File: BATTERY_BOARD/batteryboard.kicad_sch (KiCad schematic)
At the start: 32 parts, among them J1 KEYSTONE-1042, J10 Screw_Terminal_01x02, J11 Screw_Terminal_01x02, J12 Screw_Terminal_01x01, J2 KEYSTONE-1042, J3 KEYSTONE-1042, J4 KEYSTONE-1042, J5 KEYSTONE-1042, J6 KEYSTONE-1042, J7 JST_PH_S2B-PH-SM4, J8 Screw_Terminal_01x02, J9 Screw_Terminal_01x02, Q1 IRF7458, Q2 IRF7458, U1 R5460N233AF

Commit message: Battery Board Final Update
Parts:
- removed J10, J11, J8, J9: Screw_Terminal_01x02, custom-footprints:SCREWTERMINAL-3.5MM-2_LOCK, symbol Connector:Screw_Terminal_01x02
- removed J12: Screw_Terminal_01x01, Connector_PinHeader_1.00mm:PinHeader_1x01_P1.00mm_Vertical, symbol Connector:Screw_Terminal_01x01
- removed J7: JST_PH_S2B-PH-SM4, Connector_JST:JST_PH_S2B-PH-SM4-TB_1x02-1MP_P2.00mm_Horizontal, symbol Connector:Screw_Terminal_01x02
- added D4: DFLS130L, mainboard:PWRDI-123, symbol mainboard:DFLS130L
- added J10, J13, J14, J15, J16, J7, J8: SM02B-SFHRS-TF_LF__SN_, SM02BSFHRSTFLFSN, symbol SamacSys_Parts:SM02B-SFHRS-TF_LF__SN_
- added J11: F3311A7H121014E200, F3311A7H121014E200, symbol SamacSys_Parts:F3311A7H121014E200
- added K1: 9-1462038-9, 914620389, symbol SamacSys_Parts:9-1462038-9
- added Q20 (x2), Q21 (x2): NDS8434, mainboard:NDS8434, symbol mainboard:NDS8434
- added Q4 (x2), Q5 (x2): IRLML2803, mainboard:SOT-23, symbol mainboard:IRLML2803TRPBF
- added Q6: MMBT2222AT, mainboard:SOT-23, symbol mainboard:MMBT2222AT
- added R25, R27 (x2), R28 (x2): 10k, Resistor_SMD:R_0603_1608Metric, symbol mainboard:RESISTOR0603
- added R32 (x2), R33 (x2): 4.7k, Resistor_SMD:R_0603_1608Metric, symbol mainboard:RESISTOR0603
- added R37 (x2), R38 (x2): 100k, Resistor_SMD:R_0603_1608Metric, symbol mainboard:RESISTOR0603
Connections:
- net BAT_THERM: now also J11.13
- net PACK+: now also J10.2, J7.2
- net PACK- renamed GND
- net GND: now also J10.1, J11.14, J11.7, J13.1, J14.1, J15.1, J16.1, J7.1, K1.7 (NC_2), Q4.2 (S), Q4.2 (S), Q5.2 (S), Q5.2 (S), Q6.2 (E), R25.2, R27.2, R27.2, R28.2, R28.2
- new net: D4.A, K1.8 (COIL-), Q6.3 (C)
- new net: Q20.4 (Gate), Q4.3 (D), R37.1 (x2)
- new net: Q21.4 (Gate), Q5.3 (D), R38.1 (x2)
- new net: Q5.1 (G), R33.1 (x2)
- new net: Q4.1 (G), R32.1 (x2)
- new net BURN_RELAY_A: J11.8, Q6.1 (B), R25.1
- new net ENAB_BURN1: J11.9, R27.1, R32.2
- new net ENAB_BURN2: J11.10, R28.1, R33.2
- new net ENAB_BURN3: J11.11, R28.1, R33.2
- new net ENAB_BURN4: J11.12, R27.1, R32.2
- new net VBATT: D4.C, J8.1, J8.2, K1.1 (COIL+), K1.5 (NO_2)
- new net VBURN1: J14.2, Q20.5 (Drain), Q20.6 (Drain), Q20.7 (Drain), Q20.8 (Drain)
- new net VBURN2: J13.2, Q21.5 (Drain), Q21.6 (Drain), Q21.7 (Drain), Q21.8 (Drain)
- new net VBURN3: J15.2, Q21.5 (Drain), Q21.6 (Drain), Q21.7 (Drain), Q21.8 (Drain)
- new net VBURN4: J16.2, Q20.5 (Drain), Q20.6 (Drain), Q20.7 (Drain), Q20.8 (Drain)
- new net VBURN_A_IN: K1.6 (COM_2), Q20.1 (Source), Q20.1 (Source), Q20.2 (Source), Q20.2 (Source), Q20.3 (Source), Q20.3 (Source), Q21.1 (Source), Q21.1 (Source), Q21.2 (Source), Q21.2 (Source), Q21.3 (Source), Q21.3 (Source), R37.2, R37.2, R38.2, R38.2
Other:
- note added: "Burn Wire Control (Antenna Depolyment)"
- note added: "NOTE: Components labeled "do not install" (DNI) are not populated by default"
- note added: "Power Relay A"
- note removed: "Vertical or horizontal JST_PH"
- moved on the sheet: C1, C2, C3, C4, H1, H2, H3, H4, J1, J2, J3, J4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

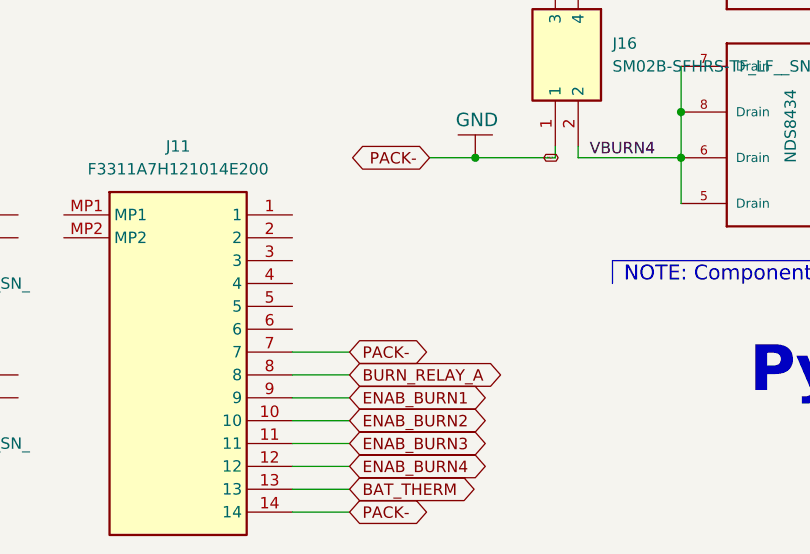
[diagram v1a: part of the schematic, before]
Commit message: Updated the FPC Connections
FPC connector is reversable now
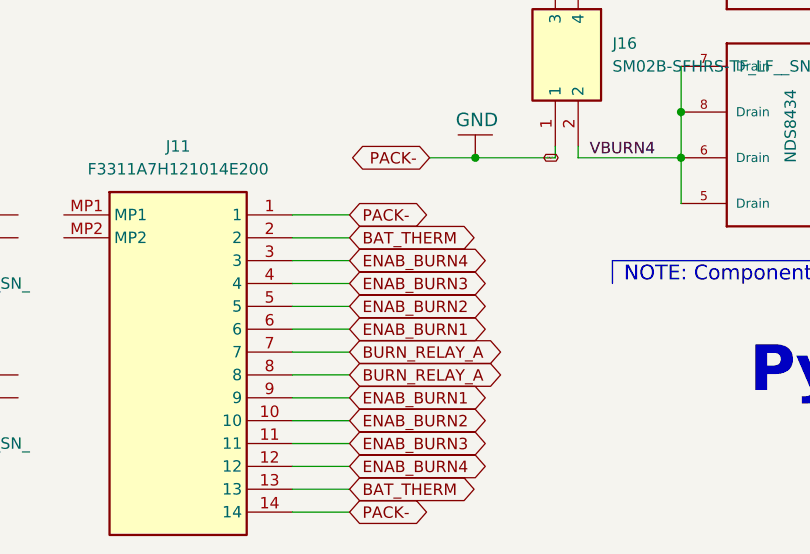
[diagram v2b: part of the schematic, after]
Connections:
- net BAT_THERM: now also J11.2
- net BURN_RELAY_A: now also J11.7
- net ENAB_BURN1: now also J11.6
- net ENAB_BURN2: now also J11.5
- net ENAB_BURN3: now also J11.4
- net ENAB_BURN4: now also J11.3
- net GND: now also J11.1; no longer J11.7
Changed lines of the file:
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@@
   (no_connect (at 44.45 151.13))
   (no_connect (at 44.45 135.89))
+  (wire (pts (xy 123.19 171.45) (xy 129.54 171.45))
+    (stroke (width 0) (type default))
+  )
   (wire (pts (xy 166.37 157.48) (xy 166.37 152.4))
     (stroke (width 0) (type default))
@@
     (stroke (width 0) (type default))
   )
+  (wire (pts (xy 123.19 173.99) (xy 129.54 173.99))
+    (stroke (width 0) (type default))
+  )
   (wire (pts (xy 198.12 99.06) (xy 205.74 99.06))
     (stroke (width 0) (type default))
@@
     (stroke (width 0) (type default))
   )
+  (wire (pts (xy 123.19 168.91) (xy 129.54 168.91))
+    (stroke (width 0) (type default))
+  )
   (wire (pts (xy 223.52 77.47) (xy 223.52 74.93))
     (stroke (width 0) (type default))
@@
     (stroke (width 0) (type default))
   )
+  (wire (pts (xy 123.19 179.07) (xy 129.54 179.07))
+    (stroke (width 0) (type default))
+  )
   (wire (pts (xy 213.36 82.55) (xy 213.36 87.63))
     (stroke (width 0) (type default))
@@
     (stroke (width 0) (type default))
   )
+  (wire (pts (xy 123.19 176.53) (xy 129.54 176.53))
+    (stroke (width 0) (type default))
+  )
   (wire (pts (xy 34.29 50.8) (xy 34.29 39.37))
     (stroke (width 0) (type default))
@@
     (stroke (width 0) (type default))
   )
-  (wire (pts (xy 123.19 179.07) (xy 129.54 179.07))
-    (stroke (width 0) (type default))
-  )
   (wire (pts (xy 205.74 104.14) (xy 205.74 101.6))
     (stroke (width 0) (type default))
@@
     (stroke (width 0) (type default))
   )
+  (wire (pts (xy 123.19 166.37) (xy 129.54 166.37))
+    (stroke (width 0) (type default))
+  )
   (wire (pts (xy 138.43 157.48) (xy 143.51 157.48))
     (stroke (width 0) (type default))
@@
   )
   (wire (pts (xy 161.29 85.09) (xy 172.72 85.09))
+    (stroke (width 0) (type default))
+  )
+  (wire (pts (xy 123.19 163.83) (xy 129.54 163.83))
     (stroke (width 0) (type default))
   )
@@
     )
   )
+  (global_label "PACK-" (shape bidirectional) (at 129.54 163.83 0)
+    (effects (font (size 1.27 1.27)) (justify left))
+    (property "Intersheetrefs" "${INTERSHEET_REFS}" (at 129.54 163.83 0)
+      (effects (font (size 1.27 1.27)) hide)
+    )
+  )
+  (global_label "BURN_RELAY_A" (shape bidirectional) (at 129.54 179.07 0)
+    (effects (font (size 1.27 1.27)) (justify left))
+    (property "Intersheetrefs" "${INTERSHEET_REFS}" (at 129.54 179.07 0)
+      (effects (font (size 1.27 1.27)) hide)
+    )
+  )
   (global_label "PACK+" (shape bidirectional) (at 100.33 104.14 270)
     (effects (font (size 1.27 1.27)) (justify right))
@@
     )
   )
+  (global_label "ENAB_BURN3" (shape bidirectional) (at 129.54 171.45 0)
+    (effects (font (size 1.27 1.27)) (justify left))
+    (property "Intersheetrefs" "${INTERSHEET_REFS}" (at 129.54 171.45 0)
+      (effects (font (size 1.27 1.27)) hide)
+    )
+  )
   (global_label "ENAB_BURN2" (shape bidirectional) (at 226.06 87.63 0)
     (effects (font (size 1.27 1.27)) (justify left))
@@
     )
   )
+  (global_label "ENAB_BURN4" (shape bidirectional) (at 129.54 168.91 0)
+    (effects (font (size 1.27 1.27)) (justify left))
+    (property "Intersheetrefs" "${INTERSHEET_REFS}" (at 129.54 168.91 0)
+      (effects (font (size 1.27 1.27)) hide)
+    )
+  )
   (global_label "BM" (shape bidirectional) (at 29.21 180.34 270)
     (effects (font (size 1.27 1.27)) (justify right))
@@
     )
   )
+  (global_label "BAT_THERM" (shape bidirectional) (at 129.54 166.37 0)
+    (effects (font (size 1.27 1.27)) (justify left))
+    (property "Intersheetrefs" "${INTERSHEET_REFS}" (at 129.54 166.37 0)
+      (effects (font (size 1.27 1.27)) hide)
+    )
+  )
   (global_label "VBATT" (shape bidirectional) (at 173.99 36.83 180)
     (effects (font (size 1.27 1.27)) (justify right))
@@
     )
   )
-  (global_label "PACK-" (shape bidirectional) (at 129.54 179.07 0)
-    (effects (font (size 1.27 1.27)) (justify left))
-    (property "Intersheetrefs" "${INTERSHEET_REFS}" (at 129.54 179.07 0)
+  (global_label "ENAB_BURN1" (shape bidirectional) (at 129.54 176.53 0)
+    (effects (font (size 1.27 1.27)) (justify left))
+    (property "Intersheetrefs" "${INTERSHEET_REFS}" (at 129.54 176.53 0)
       (effects (font (size 1.27 1.27)) hide)
     )
@@
       (effects (font (size 1.27 1.27)) hide)
     )
+  )
+  (global_label "ENAB_BURN2" (shape bidirectional) (at 129.54 173.99 0)
+    (effects (font (size 1.27 1.27)) (justify left))
+    (property "Intersheetrefs" "${INTERSHEET_REFS}" (at 129.54 173.99 0)
+      (effects (font (size 1.27 1.27)) hide)
+    )

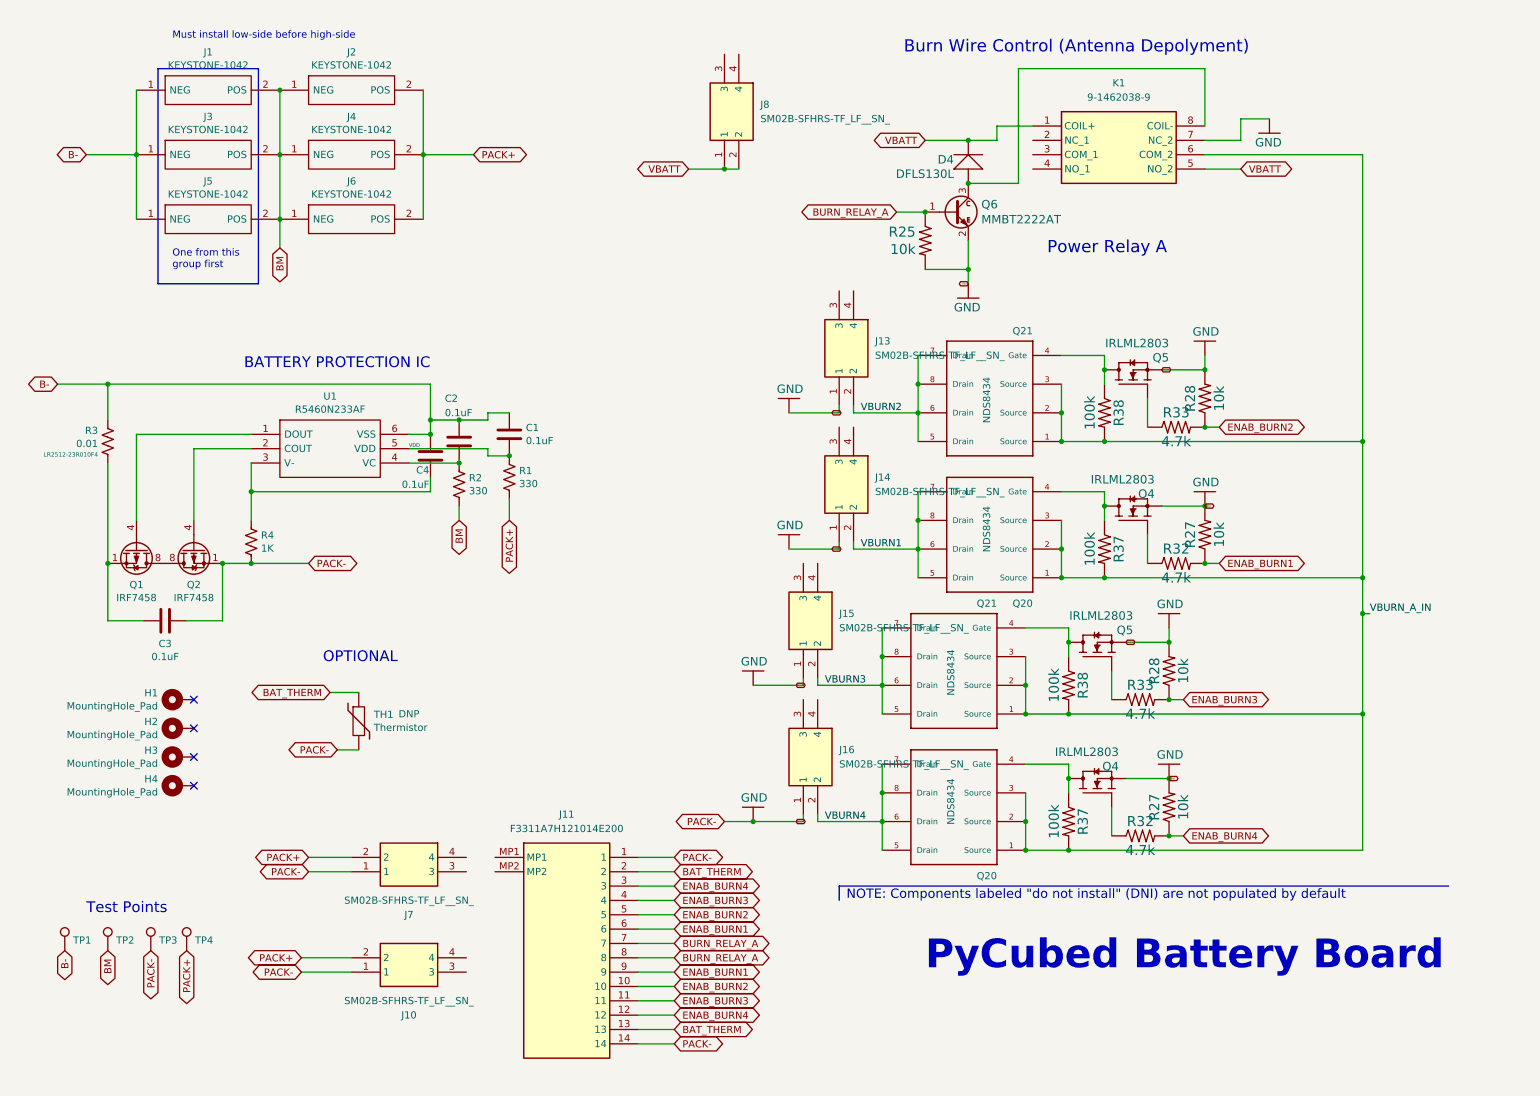
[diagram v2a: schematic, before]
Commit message: Battery Board Updated based on Feedback
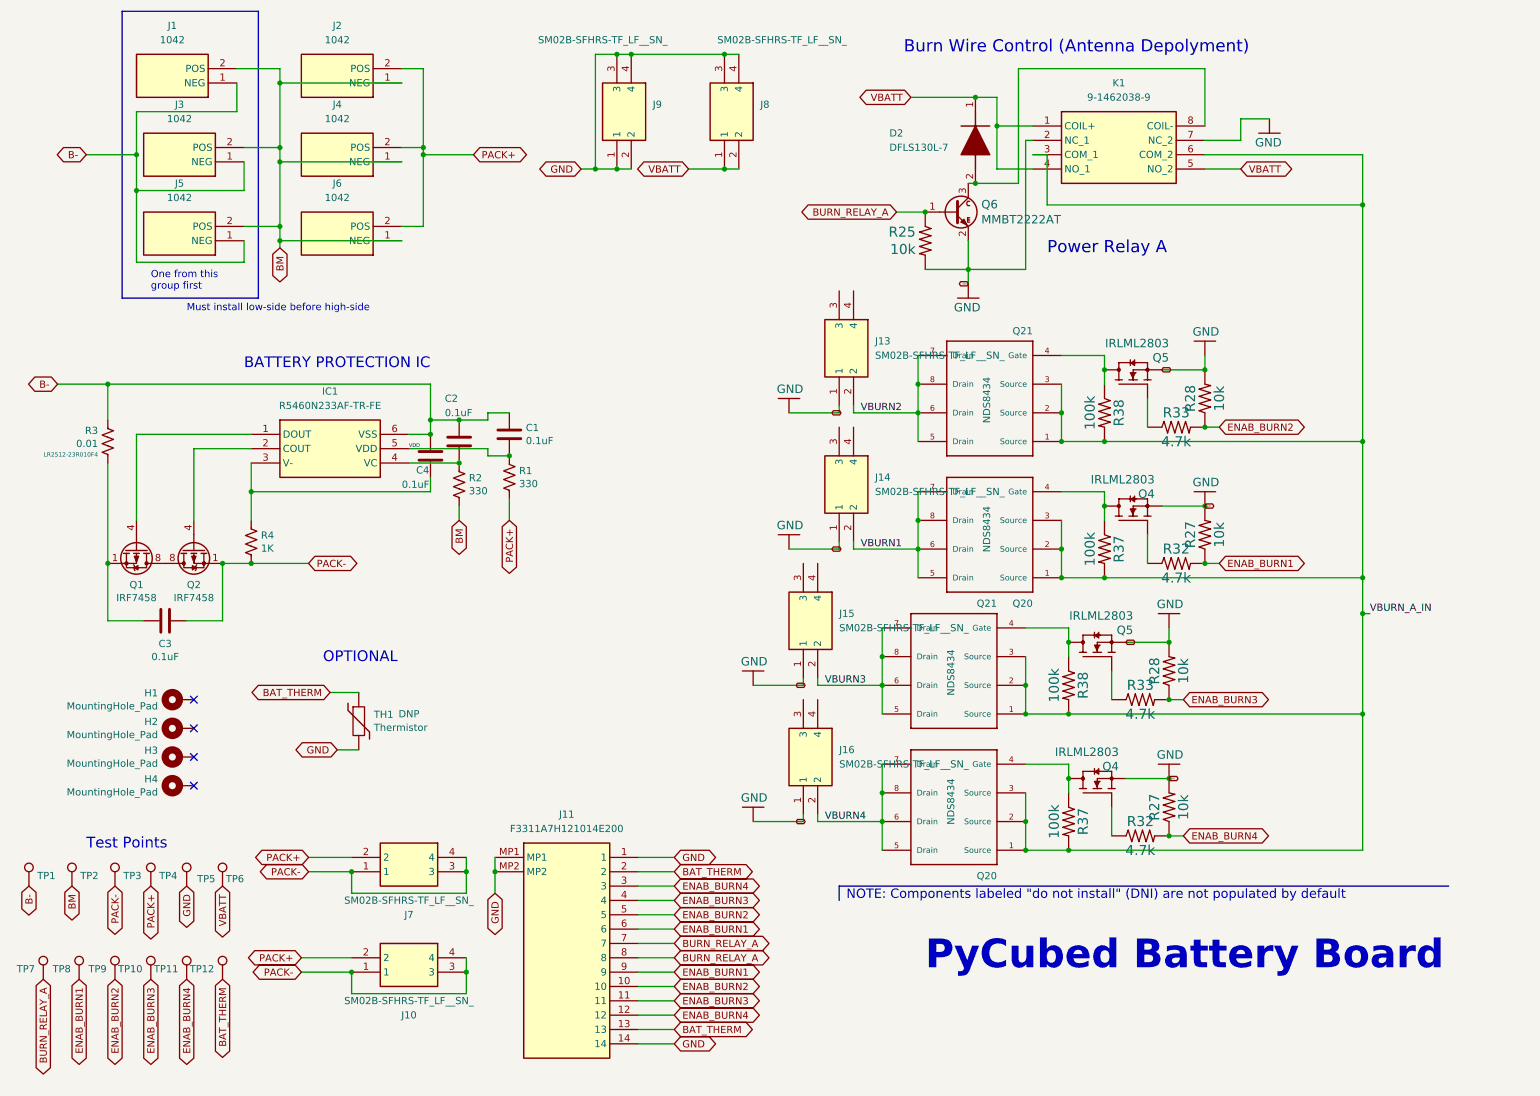
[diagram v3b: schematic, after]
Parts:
- removed D4: DFLS130L, mainboard:PWRDI-123, symbol mainboard:DFLS130L
- removed J1, J2, J3, J4, J5, J6: KEYSTONE-1042, custom-footprints:KEYSTONE-1042, symbol batteryboard-rescue:1042-symbols
- removed U1: R5460N233AF, custom-footprints:SOT95P280X130-6N, symbol batteryboard-rescue:R5460N233AF-symbols
- added D2: DFLS130L-7, POWERDI_123, symbol SamacSys_Parts:DFLS130L-7
- added IC1: R5460N233AF-TR-FE, SOT95P280X140-6N, symbol SamacSys_Parts:R5460N233AF-TR-FE
- added J1, J2, J3, J4, J5, J6: 1042, KEYSTONE-1042, symbol SamacSys_Parts:1042
- added J9: SM02B-SFHRS-TF_LF__SN_, SM02BSFHRSTFLFSN, symbol SamacSys_Parts:SM02B-SFHRS-TF_LF__SN_
- added TP10, TP11, TP12, TP5, TP6, TP7, TP8, TP9: TestPoint, TestPoint:TestPoint_Loop_D1.80mm_Drill1.0mm_Beaded, symbol Connector:TestPoint
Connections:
- net B-: now also IC1.6 (VSS), J1.1 (NEG), J3.1 (NEG), J5.1 (NEG)
- net BAT_THERM: now also TP12.1
- net BM: now also J1.2 (POS), J2.1 (NEG), J3.2 (POS), J4.1 (NEG), J5.2 (POS), J6.1 (NEG)
- net BURN_RELAY_A: now also TP7.1
- net ENAB_BURN1: now also TP8.1
- net ENAB_BURN2: now also TP9.1
- net ENAB_BURN3: now also TP10.1
- net ENAB_BURN4: now also TP11.1
- net GND: now also J11.MP1, J11.MP2, J8.3, J8.4, K1.2 (NC_1), J9.1, J9.2, J9.3, J9.4, TP5.1; no longer C3.2, J10.1, J7.1, Q2.1 (S), Q2.2 (S), Q2.3 (S), R4.2, TP3.1
- net PACK+: now also J2.2 (POS), J4.2 (POS), J6.2 (POS)
- net VBATT: now also K1.4 (NO_1), D2.1 (K), TP6.1
- net VBURN_A_IN: now also K1.3 (COM_1)
- net VDD: now also IC1.5 (VDD)
- net at Q1.4 (G): now also IC1.1 (DOUT)
- net at Q2.4 (G): now also IC1.2 (COUT)
- net at C4.2, R4.1: now also IC1.3 (V-)
- net at C2.2, R2.2: now also IC1.4 (VC)
- net at K1.8 (COIL-), Q6.3 (C): now also D2.2 (A)
- net PACK-: now reaches J10.3
- net PACK-: now also C3.2, J10.1, J10.4, J7.1, J7.3, J7.4, Q2.1 (S), Q2.2 (S), Q2.3 (S), R4.2, TP3.1
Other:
- moved on the sheet: TP1, TP2, TP3, TP4
